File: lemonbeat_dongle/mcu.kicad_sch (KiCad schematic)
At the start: 44 parts, among them J201 USB_A, J202 Prog, J203 u.FL, SW201 SW_Push, U201 nRF52840, Y201 32MHz, Y202 32.768kHz

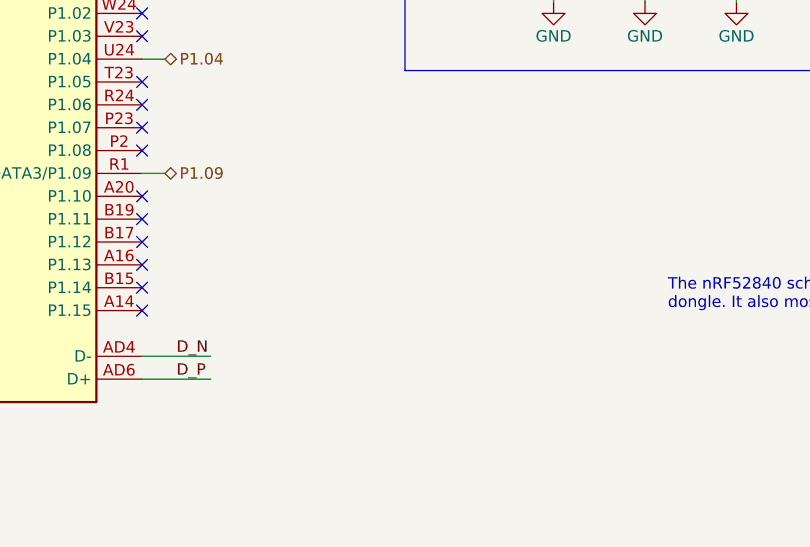
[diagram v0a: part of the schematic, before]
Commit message: dongle: add some LEDs
- power LED (connected to VBUS, constantly on if USB is powered)
- TX LED (GPIO2)
- RX LED (GPIO3)
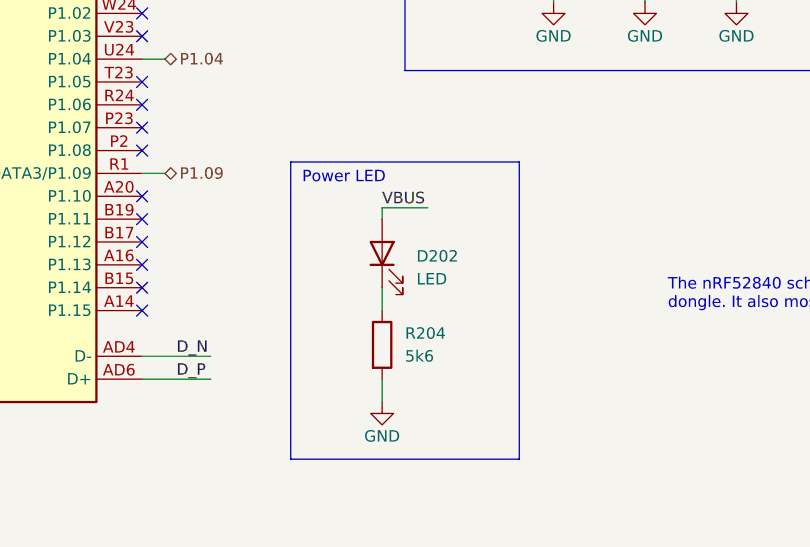
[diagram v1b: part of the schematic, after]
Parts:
- added D202: LED, LED_SMD:LED_0805_2012Metric, symbol Device:LED
- added R204: 5k6, Resistor_SMD:R_0402_1005Metric, symbol Device:R
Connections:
- net GND: now also R204.2
- net VBUS: now also D202.2 (A)
- new net: D202.1 (K), R204.1
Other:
- note added: "Power LED"
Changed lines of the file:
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@@
+    (stroke (width 0) (type default) (color 0 0 0 0))
+  )
+  (wire (pts (xy 148.59 162.56) (xy 153.67 162.56))
     (stroke (width 0) (type default) (color 0 0 0 0))
   )
@@
     (stroke (width 0) (type default) (color 0 0 0 0))
   )
+  (polyline (pts (xy 163.83 190.5) (xy 138.43 190.5))
+    (stroke (width 0) (type default) (color 0 0 0 0))
+  )
   (polyline (pts (xy 184.15 35.56) (xy 184.15 114.3))
     (stroke (width 0) (type default) (color 0 0 0 0))
@@
     (stroke (width 0) (type default) (color 0 0 0 0))
   )
+  (wire (pts (xy 148.59 171.45) (xy 148.59 173.99))
+    (stroke (width 0) (type default) (color 0 0 0 0))
+  )
   (polyline (pts (xy 54.61 101.6) (xy 54.61 135.89))
     (stroke (width 0) (type default) (color 0 0 0 0))
@@
     (stroke (width 0) (type default) (color 0 0 0 0))
   )
+  (polyline (pts (xy 138.43 157.48) (xy 138.43 190.5))
+    (stroke (width 0) (type default) (color 0 0 0 0))
+  )
   (wire (pts (xy 127 60.96) (xy 133.35 60.96))
     (stroke (width 0) (type default) (color 0 0 0 0))
   )
+  (wire (pts (xy 148.59 181.61) (xy 148.59 184.15))
+    (stroke (width 0) (type default) (color 0 0 0 0))
+  )
   (wire (pts (xy 121.92 74.93) (xy 124.46 74.93))
     (stroke (width 0) (type default) (color 0 0 0 0))
@@
     (stroke (width 0) (type default) (color 0 0 0 0))
   )
+  (polyline (pts (xy 138.43 157.48) (xy 163.83 157.48))
+    (stroke (width 0) (type default) (color 0 0 0 0))
+  )
   (wire (pts (xy 21.59 113.03) (xy 21.59 123.19))
     (stroke (width 0) (type default) (color 0 0 0 0))
@@
     (stroke (width 0) (type default) (color 0 0 0 0))
   )
+  (wire (pts (xy 148.59 163.83) (xy 148.59 162.56))
+    (stroke (width 0) (type default) (color 0 0 0 0))
+  )
   (wire (pts (xy 133.35 60.96) (xy 133.35 59.69))
     (stroke (width 0) (type default) (color 0 0 0 0))
@@
   )
   (wire (pts (xy 19.05 91.44) (xy 19.05 92.71))
+    (stroke (width 0) (type default) (color 0 0 0 0))
+  )
+  (polyline (pts (xy 163.83 157.48) (xy 163.83 190.5))
     (stroke (width 0) (type default) (color 0 0 0 0))
   )
@@
     (effects (font (size 1.27 1.27)) (justify left bottom))
   )
+  (text "Power LED" (at 139.7 160.02 0)
+    (effects (font (size 1.27 1.27)) (justify left bottom))
+  )
   (text "LFXO\n(Optional)" (at 158.75 54.61 0)
     (effects (font (size 1.27 1.27)) (justify left bottom))
@@
   )
   (label "SWDIO" (at 257.81 128.27 0)
+    (effects (font (size 1.27 1.27)) (justify left bottom))
+  )
+  (label "VBUS" (at 148.59 162.56 0)
     (effects (font (size 1.27 1.27)) (justify left bottom))
   )
@@
     (pin "1")
     (pin "2")
+  )
+  (symbol (lib_id "power:GND") (at 148.59 184.15 0) (unit 1)
+    (in_bom yes) (on_board yes)
+    (property "Reference" "#PWR0235" (id 0) (at 148.59 190.5 0)
+      (effects (font (size 1.27 1.27)) hide)
+    )
+    (property "Value" "GND" (id 1) (at 148.59 187.96 0))
+    (property "Footprint" "" (id 2) (at 148.59 184.15 0)
+      (effects (font (size 1.27 1.27)) hide)
+    )
+    (property "Datasheet" "" (id 3) (at 148.59 184.15 0)
+      (effects (font (size 1.27 1.27)) hide)
+    )
+    (pin "1")
   )
   (symbol (lib_id "power:GND") (at 113.03 27.94 0) (unit 1)
@@
     (pin "1")
   )
+  (symbol (lib_id "Device:R") (at 148.59 177.8 0) (unit 1)
+    (in_bom yes) (on_board yes) (fields_autoplaced)
+    (property "Reference" "R204" (id 0) (at 151.13 176.5299 0)
+      (effects (font (size 1.27 1.27)) (justify left))
+    )
+    (property "Value" "5k6" (id 1) (at 151.13 179.0699 0)
+      (effects (font (size 1.27 1.27)) (justify left))
+    )
+    (property "Footprint" "Resistor_SMD:R_0402_1005Metric" (id 2) (at 146.812 177.8 90)
+      (effects (font (size 1.27 1.27)) hide)
+    )
+    (property "Datasheet" "https://datasheet.lcsc.com/lcsc/2206010045_UNI-ROYAL-Uniroyal-Elec-0402WGF5601TCE_C25908.pdf" (id 3) (at 148.59 177.8 0)
+      (effects (font (size 1.27 1.27)) hide)
+    )
+    (property "Comment" "JLCPCB basic part" (id 4) (at 148.59 177.8 0)
+      (effects (font (size 1.27 1.27)) hide)
+    )
+    (property "Description" "62.5mW Thick Film Resistors 50V ±100ppm/℃ ±1% -55℃~+155℃ 5.6kΩ 0402 Chip Resistor" (id 5) (at 148.59 177.8 0)
+      (effects (font (size 1.27 1.27)) hide)
+    )
+    (property "LCSC" "C25908" (id 6) (at 148.59 177.8 0)
+      (effects (font (size 1.27 1.27)) hide)
+    )
+    (property "Manufacturer" "Uniroyal Elec" (id 7) (at 148.59 177.8 0)
+      (effects (font (size 1.27 1.27)) hide)
+    )
+    (property "Part Number" "0402WGF5601TCE" (id 8) (at 148.59 177.8 0)
+      (effects (font (size 1.27 1.27)) hide)
+    )
+    (pin "1")
+    (pin "2")
+  )
   (symbol (lib_id "power:GND") (at 177.8 139.7 0) (unit 1)
     (in_bom yes) (on_board yes)
@@
     (pin "1")
   )
+  (symbol (lib_id "Device:LED") (at 148.59 167.64 90) (unit 1)
+    (in_bom yes) (on_board yes) (fields_autoplaced)
+    (property "Reference" "D202" (id 0) (at 152.4 167.9574 90)
+      (effects (font (size 1.27 1.27)) (justify right))
+    )
+    (property "Value" "LED" (id 1) (at 152.4 170.4974 90)
+      (effects (font (size 1.27 1.27)) (justify right))
+    )
+    (property "Footprint" "LED_SMD:LED_0805_2012Metric" (id 2) (at 148.59 167.64 0)
+      (effects (font (size 1.27 1.27)) hide)
+    )
+    (property "Datasheet" "https://datasheet.lcsc.com/lcsc/2008201032_Foshan-NationStar-Optoelectronics-NCD0805R1_C84256.pdf" (id 3) (at 148.59 167.64 0)
+      (effects (font (size 1.27 1.27)) hide)
+    )
+    (property "Comment" "JLCPCB basic part" (id 4) (at 148.59 167.64 0)
+      (effects (font (size 1.27 1.27)) hide)
+    )
+    (property "Description" "Red 0805 Light Emitting Diodes (LED) ROHS" (id 5) (at 148.59 167.64 0)
+      (effects (font (size 1.27 1.27)) hide)
+    )
+    (property "LCSC" "C84256" (id 6) (at 148.59 167.64 0)
+      (effects (font (size 1.27 1.27)) hide)
+    )
+    (property "Manufacturer" "Foshan NationStar Optoelectronics" (id 7) (at 148.59 167.64 0)
+      (effects (font (size 1.27 1.27)) hide)
+    )
+    (property "Part Number" "NCD0805R1" (id 8) (at 148.59 167.64 0)
+      (effects (font (size 1.27 1.27)) hide)
+    )
+    (pin "1")
+    (pin "2")
+  )
   (symbol (lib_id "Device:FerriteBead") (at 229.87 50.8 90) (unit 1)

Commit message: dongle: schematic: add comment regarding C222
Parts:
- C222: Comment (none) -> Exists in dongle schematic, but N.C. in reference circuit f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
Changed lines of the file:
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@@
+      (effects (font (size 1.27 1.27)) hide)
+    )
+    (property "Comment" "Exists in dongle schematic, but N.C. in reference circuit from datasheet. Only relevant for DCDC mode." (id 8) (at 27.94 67.31 0)
       (effects (font (size 1.27 1.27)) hide)
     )

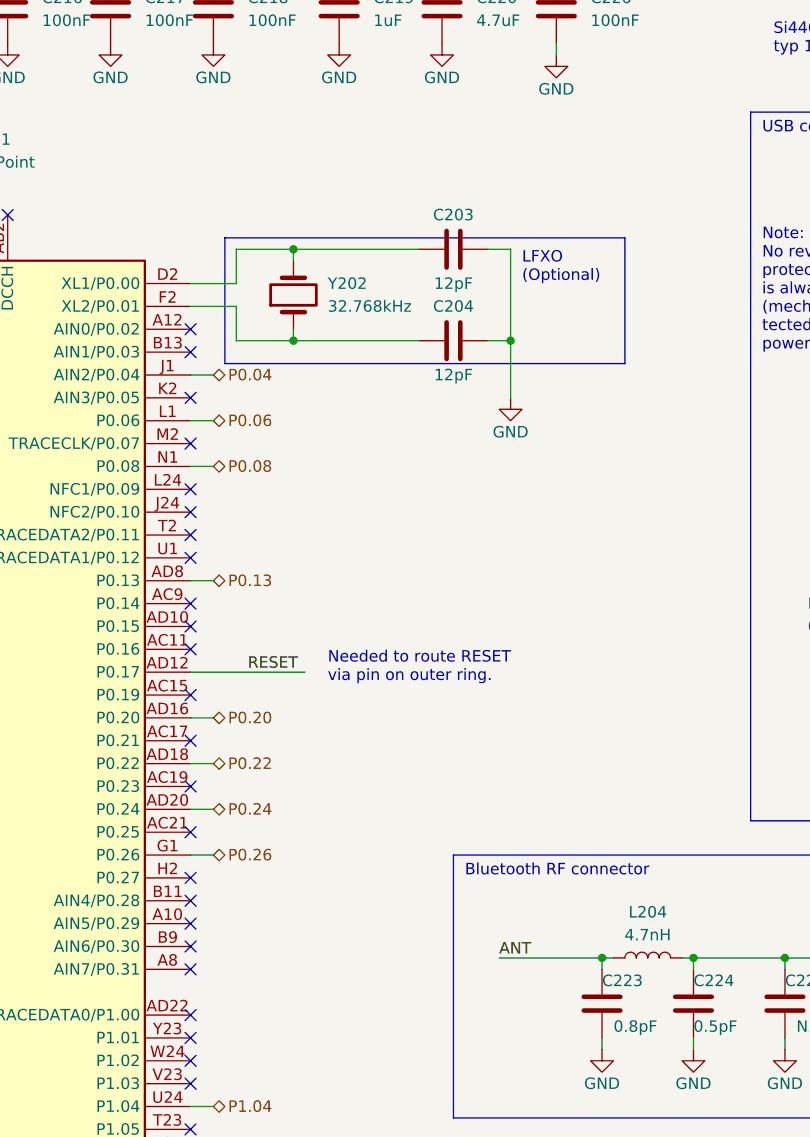
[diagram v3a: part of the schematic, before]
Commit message: dongle: schematic: additional test points for nRF52840
These can be used for a UART or as GPIO.
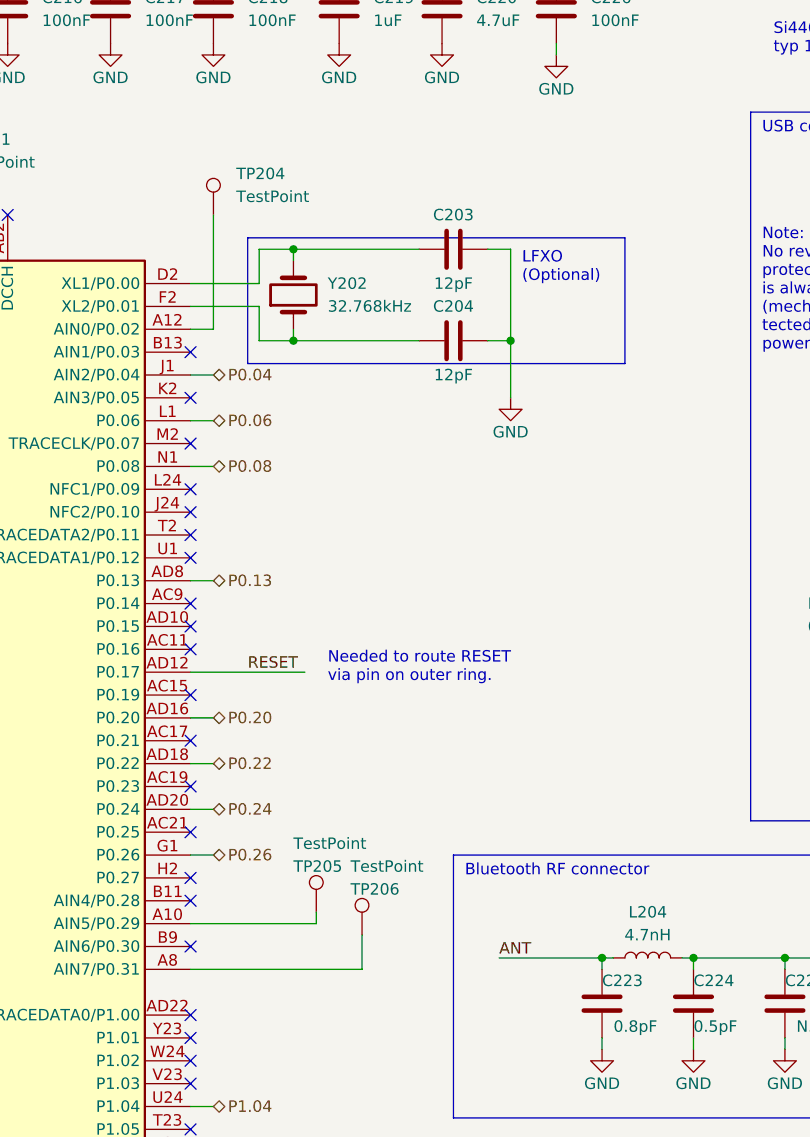
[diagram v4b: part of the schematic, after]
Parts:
- added TP204, TP205, TP206: TestPoint, TestPoint:TestPoint_Pad_D1.0mm, symbol Connector:TestPoint
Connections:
- net at U201.A10 (AIN5/P0.29): now also TP205.1
- net at U201.A12 (AIN0/P0.02): now also TP204.1
- net at U201.A8 (AIN7/P0.31): now also TP206.1
- no-connect marks 39 -> 36
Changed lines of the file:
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@@
   (no_connect (at 121.92 105.41))
   (no_connect (at 121.92 67.31))
-  (no_connect (at 121.92 59.69))
   (no_connect (at 121.92 62.23))
   (no_connect (at 121.92 143.51))
@@
   (no_connect (at 121.92 123.19))
   (no_connect (at 121.92 92.71))
-  (no_connect (at 121.92 130.81))
   (no_connect (at 121.92 128.27))
   (no_connect (at 121.92 120.65))
-  (no_connect (at 121.92 125.73))
   (no_connect (at 121.92 100.33))
   (no_connect (at 121.92 168.91))
@@
     (stroke (width 0) (type default) (color 0 0 0 0))
   )
-  (wire (pts (xy 121.92 57.15) (xy 127 57.15))
+  (wire (pts (xy 121.92 57.15) (xy 129.54 57.15))
     (stroke (width 0) (type default) (color 0 0 0 0))
   )
@@
     (stroke (width 0) (type default) (color 0 0 0 0))
   )
-  (polyline (pts (xy 125.73 49.53) (xy 170.18 49.53))
+  (polyline (pts (xy 128.27 49.53) (xy 170.18 49.53))
     (stroke (width 0) (type default) (color 0 0 0 0))
   )
@@
     (stroke (width 0) (type default) (color 0 0 0 0))
   )
-  (wire (pts (xy 127 50.8) (xy 133.35 50.8))
+  (wire (pts (xy 129.54 50.8) (xy 133.35 50.8))
     (stroke (width 0) (type default) (color 0 0 0 0))
   )
@@
     (stroke (width 0) (type default) (color 0 0 0 0))
   )
-  (polyline (pts (xy 125.73 49.53) (xy 125.73 63.5))
+  (polyline (pts (xy 128.27 49.53) (xy 128.27 63.5))
     (stroke (width 0) (type default) (color 0 0 0 0))
   )
@@
     (stroke (width 0) (type default) (color 0 0 0 0))
   )
+  (wire (pts (xy 135.89 125.73) (xy 135.89 124.46))
+    (stroke (width 0) (type default) (color 0 0 0 0))
+  )
   (polyline (pts (xy 138.43 157.48) (xy 138.43 190.5))
     (stroke (width 0) (type default) (color 0 0 0 0))
   )
-  (wire (pts (xy 127 60.96) (xy 133.35 60.96))
+  (wire (pts (xy 129.54 60.96) (xy 133.35 60.96))
     (stroke (width 0) (type default) (color 0 0 0 0))
   )
@@
     (stroke (width 0) (type default) (color 0 0 0 0))
   )
+  (wire (pts (xy 121.92 59.69) (xy 124.46 59.69))
+    (stroke (width 0) (type default) (color 0 0 0 0))
+  )
   (wire (pts (xy 176.53 129.54) (xy 177.8 129.54))
     (stroke (width 0) (type default) (color 0 0 0 0))
@@
     (stroke (width 0) (type default) (color 0 0 0 0))
   )
+  (wire (pts (xy 121.92 130.81) (xy 140.97 130.81))
+    (stroke (width 0) (type default) (color 0 0 0 0))
+  )
   (polyline (pts (xy 54.61 135.89) (xy 17.78 135.89))
     (stroke (width 0) (type default) (color 0 0 0 0))
@@
     (stroke (width 0) (type default) (color 0 0 0 0))
   )
-  (wire (pts (xy 127 57.15) (xy 127 60.96))
+  (wire (pts (xy 129.54 57.15) (xy 129.54 60.96))
     (stroke (width 0) (type default) (color 0 0 0 0))
   )
@@
     (stroke (width 0) (type default) (color 0 0 0 0))
   )
+  (wire (pts (xy 140.97 130.81) (xy 140.97 127))
+    (stroke (width 0) (type default) (color 0 0 0 0))
+  )
   (wire (pts (xy 43.18 114.3) (xy 43.18 113.03))
     (stroke (width 0) (type default) (color 0 0 0 0))
@@
     (stroke (width 0) (type default) (color 0 0 0 0))
   )
-  (wire (pts (xy 121.92 54.61) (xy 127 54.61))
+  (wire (pts (xy 121.92 54.61) (xy 129.54 54.61))
     (stroke (width 0) (type default) (color 0 0 0 0))
   )
@@
     (stroke (width 0) (type default) (color 0 0 0 0))
   )
+  (wire (pts (xy 124.46 59.69) (xy 124.46 46.99))
+    (stroke (width 0) (type default) (color 0 0 0 0))
+  )
   (wire (pts (xy 69.85 21.59) (xy 69.85 22.86))
     (stroke (width 0) (type default) (color 0 0 0 0))
@@
     (stroke (width 0) (type default) (color 0 0 0 0))
   )
-  (wire (pts (xy 127 54.61) (xy 127 50.8))
+  (wire (pts (xy 129.54 54.61) (xy 129.54 50.8))
     (stroke (width 0) (type default) (color 0 0 0 0))
   )
@@
     (stroke (width 0) (type default) (color 0 0 0 0))
   )
+  (wire (pts (xy 121.92 125.73) (xy 135.89 125.73))
+    (stroke (width 0) (type default) (color 0 0 0 0))
+  )
   (wire (pts (xy 27.94 62.23) (xy 43.18 62.23))
     (stroke (width 0) (type default) (color 0 0 0 0))
@@
     (stroke (width 0) (type default) (color 0 0 0 0))
   )
-  (polyline (pts (xy 170.18 63.5) (xy 125.73 63.5))
+  (polyline (pts (xy 170.18 63.5) (xy 128.27 63.5))
     (stroke (width 0) (type default) (color 0 0 0 0))
   )
@@
     (pin "1")
   )
+  (symbol (lib_id "Connector:TestPoint") (at 135.89 124.46 0) (unit 1)
+    (in_bom yes) (on_board yes)
+    (property "Reference" "TP205" (id 0) (at 133.35 119.38 0)
+      (effects (font (size 1.27 1.27)) (justify left))
+    )
+    (property "Value" "TestPoint" (id 1) (at 133.35 116.84 0)
+      (effects (font (size 1.27 1.27)) (justify left))
+    )
+    (property "Footprint" "TestPoint:TestPoint_Pad_D1.0mm" (id 2) (at 140.97 124.46 0)
+      (effects (font (size 1.27 1.27)) hide)
+    )
+    (property "Datasheet" "~" (id 3) (at 140.97 124.46 0)
+      (effects (font (size 1.27 1.27)) hide)
+    )
+    (pin "1")
+  )
   (symbol (lib_id "Device:C") (at 223.52 57.15 0) (unit 1)
     (in_bom yes) (on_board yes) (fields_autoplaced)
@@
     (pin "2")
   )
+  (symbol (lib_id "Connector:TestPoint") (at 124.46 46.99 0) (unit 1)
+    (in_bom yes) (on_board yes) (fields_autoplaced)
+    (property "Reference" "TP204" (id 0) (at 127 42.4179 0)
+      (effects (font (size 1.27 1.27)) (justify left))
+    )
+    (property "Value" "TestPoint" (id 1) (at 127 44.9579 0)
+      (effects (font (size 1.27 1.27)) (justify left))
+    )
+    (property "Footprint" "TestPoint:TestPoint_Pad_D1.0mm" (id 2) (at 129.54 46.99 0)
+      (effects (font (size 1.27 1.27)) hide)
+    )
+    (property "Datasheet" "~" (id 3) (at 129.54 46.99 0)
+      (effects (font (size 1.27 1.27)) hide)
+    )
+    (pin "1")
+  )
   (symbol (lib_id "power:PWR_FLAG") (at 245.11 69.85 0) (unit 1)
     (in_bom yes) (on_board yes)
@@
       (effects (font (size 1.27 1.27)) hide)
     )
+    (pin "1")
+  )
+  (symbol (lib_id "Connector:TestPoint") (at 140.97 127 0) (unit 1)
+    (in_bom yes) (on_board yes)
+    (property "Reference" "TP206" (id 0) (at 139.7 121.92 0)
+      (effects (font (size 1.27 1.27)) (justify left))
+    )
+    (property "Value" "TestPoint" (id 1) (at 139.7 119.38 0)
+      (effects (font (size 1.27 1.27)) (justify left))
+    )
+    (property "Footprint" "TestPoint:TestPoint_Pad_D1.0mm" (id 2) (at 146.05 127 0)
+      (effects (font (size 1.27 1.27)) hide)
+    )
+    (property "Datasheet" "~" (id 3) (at 146.05 127 0)
+      (effects (font (size 1.27 1.27)) hide)
+    )
